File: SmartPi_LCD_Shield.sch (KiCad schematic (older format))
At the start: 47 parts, among them J1 Ant_SMA, J3 Micro_SD_Card, J4 Conn_01x02, J5 Conn_01x16, Q1 BC547, SW1 Reset, SW2 UP, SW3 LEFT, SW4 RIGHT, SW5 SELECT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

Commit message: finished routing
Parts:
- added CreativeCommonsPublicDomain1: License, Symbol:Symbol_CreativeCommonsPublicDomain_SilkScreenTop_Small, symbol Connector:TestPoint
- added J2: Conn_01x01, Connector_PinSocket_2.54mm:PinSocket_1x01_P2.54mm_Vertical, symbol Connector_Generic:Conn_01x01
- added KiCad1: License, Symbol:KiCad-Logo2_8mm_SilkScreen, symbol Connector:TestPoint
- added RV2: 10k, Potentiometer_THT:Potentiometer_Bourns_3296X_Horizontal, symbol Device:R_POT
- LOGO1: footprint Symbol:OSHW-Logo2_7.3x6mm_SilkScreen -> Symbol:OSHW-Logo2_14.6x12mm_SilkScreen
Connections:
- net +5V: now also RV2.3
- net GND: now also RV2.1
- net at DS1.3 (VO), RV1.2: now also RV2.2
- net at J1.1 (Pin_1), U1.9 (ANT): now also J2.1 (Pin_1)
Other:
- moved on the sheet: J1
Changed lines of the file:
@@
-EESchema Schematic File Version 5
+EESchema Schematic File Version 4
+LIBS:SmartPi_LCD_Shield-cache
 EELAYER 29 0
 EELAYER END
@@
 U 1 1 5CDA4BA3
 P 2750 5400
-F 0 "RV1" H 2680 5354 50  0000 R CNN
-F 1 "10k" H 2680 5445 50  0000 R CNN
+F 0 "RV1" H 2500 5450 50  0000 R CNN
+F 1 "10k" H 2500 5350 50  0000 R CNN
 F 2 "Potentiometer_THT:Potentiometer_Bourns_3266P_Horizontal" H 2750 5400 50  0001 C CNN
 F 3 "~" H 2750 5400 50  0001 C CNN
@@
 L Connector_Generic:Conn_01x02 J1
 U 1 1 5D0CF337
-P 6700 1400
-F 0 "J1" H 6618 1075 50  0000 C CNN
-F 1 "Ant_SMA" H 6618 1166 50  0000 C CNN
-F 2 "Connector_Coaxial:SMA_Amphenol_132289_EdgeMount" H 6700 1400 50  0001 C CNN
-F 3 "~" H 6700 1400 50  0001 C CNN
-	1    6700 1400
+P 7250 1400
+F 0 "J1" H 7168 1075 50  0000 C CNN
+F 1 "Ant_SMA" H 7168 1166 50  0000 C CNN
+F 2 "Connector_Coaxial:SMA_Amphenol_132289_EdgeMount" H 7250 1400 50  0001 C CNN
+F 3 "~" H 7250 1400 50  0001 C CNN
+	1    7250 1400
 	1    0    0    1
 $EndComp
@@
 L power:GND #PWR03
 U 1 1 5D0D7020
-P 6400 1100
-F 0 "#PWR03" H 6400 850 50  0001 C CNN
-F 1 "GND" V 6400 900 50  0000 C CNN
-F 2 "" H 6400 1100 50  0001 C CNN
-F 3 "" H 6400 1100 50  0001 C CNN
-	1    6400 1100
+P 6950 1100
+F 0 "#PWR03" H 6950 850 50  0001 C CNN
+F 1 "GND" V 6950 900 50  0000 C CNN
+F 2 "" H 6950 1100 50  0001 C CNN
+F 3 "" H 6950 1100 50  0001 C CNN
+	1    6950 1100
 	-1   0    0    1
 $EndComp
 Wire Wire Line
-	6500 1300 6400 1300
+	7050 1300 6950 1300
 Wire Wire Line
 	5700 3900 5250 3900
@@
 $EndComp
 Wire Wire Line
-	6250 1400 6500 1400
-Wire Wire Line
-	6400 1100 6400 1300
+	6950 1100 6950 1300
 $Comp
 L Graphic:Logo_Open_Hardware_Small LOGO1
@@
 F 0 "LOGO1" H 7300 7125 50  0001 C CNN
 F 1 "Logo_Open_Hardware_Small" H 7300 6625 50  0001 C CNN
-F 2 "Symbol:OSHW-Logo2_7.3x6mm_SilkScreen" H 7300 6850 50  0001 C CNN
+F 2 "Symbol:OSHW-Logo2_14.6x12mm_SilkScreen" H 7300 6850 50  0001 C CNN
 F 3 "~" H 7300 6850 50  0001 C CNN
 	1    7300 6850
 	1    0    0    -1
 $EndComp
+$Comp
+L Connector_Generic:Conn_01x01 J2
+U 1 1 5CD99C08
+P 6500 1050
+F 0 "J2" V 6418 962 50  0000 R CNN
+F 1 "Conn_01x01" V 6373 962 50  0001 R CNN
+F 2 "Connector_PinSocket_2.54mm:PinSocket_1x01_P2.54mm_Vertical" H 6500 1050 50  0001 C CNN
+F 3 "~" H 6500 1050 50  0001 C CNN
+	1    6500 1050
+	0    -1   -1   0
+$EndComp
+Wire Wire Line
+	6250 1400 6500 1400
+Wire Wire Line
+	6500 1250 6500 1400
+Connection ~ 6500 1400
+Wire Wire Line
+	6500 1400 7050 1400
+$Comp
+L Device:R_POT RV2
+U 1 1 5CDAF2AC
+P 2750 5400
+F 0 "RV2" H 2680 5354 50  0000 R CNN
+F 1 "10k" H 2680 5445 50  0000 R CNN
+F 2 "Potentiometer_THT:Potentiometer_Bourns_3296X_Horizontal" H 2750 5400 50  0001 C CNN
+F 3 "~" H 2750 5400 50  0001 C CNN
+	1    2750 5400
+	-1   0    0    -1
+$EndComp
+Connection ~ 2750 5250
+Connection ~ 2600 5400
+Connection ~ 2750 5550
+$Comp
+L Connector:TestPoint CreativeCommonsPublicDomain1
+U 1 1 5CDBC513
+P 8000 6800
+F 0 "CreativeCommonsPublicDomain1" H 8058 6872 50  0000 L CNN
+F 1 "License" H 8058 6827 50  0001 L CNN
+F 2 "Symbol:Symbol_CreativeCommonsPublicDomain_SilkScreenTop_Small" H 8200 6800 50  0001 C CNN
+F 3 "~" H 8200 6800 50  0001 C CNN
+	1    8000 6800
+	1    0    0    -1
+$EndComp
+$Comp
+L Connector:TestPoint KiCad1
+U 1 1 5CDBD805
+P 8000 7050
+F 0 "KiCad1" H 8058 7122 50  0000 L CNN
+F 1 "License" H 8058 7077 50  0001 L CNN
+F 2 "Symbol:KiCad-Logo2_8mm_SilkScreen" H 8200 7050 50  0001 C CNN
+F 3 "~" H 8200 7050 50  0001 C CNN
+	1    8000 7050
+	1    0    0    -1
+$EndComp

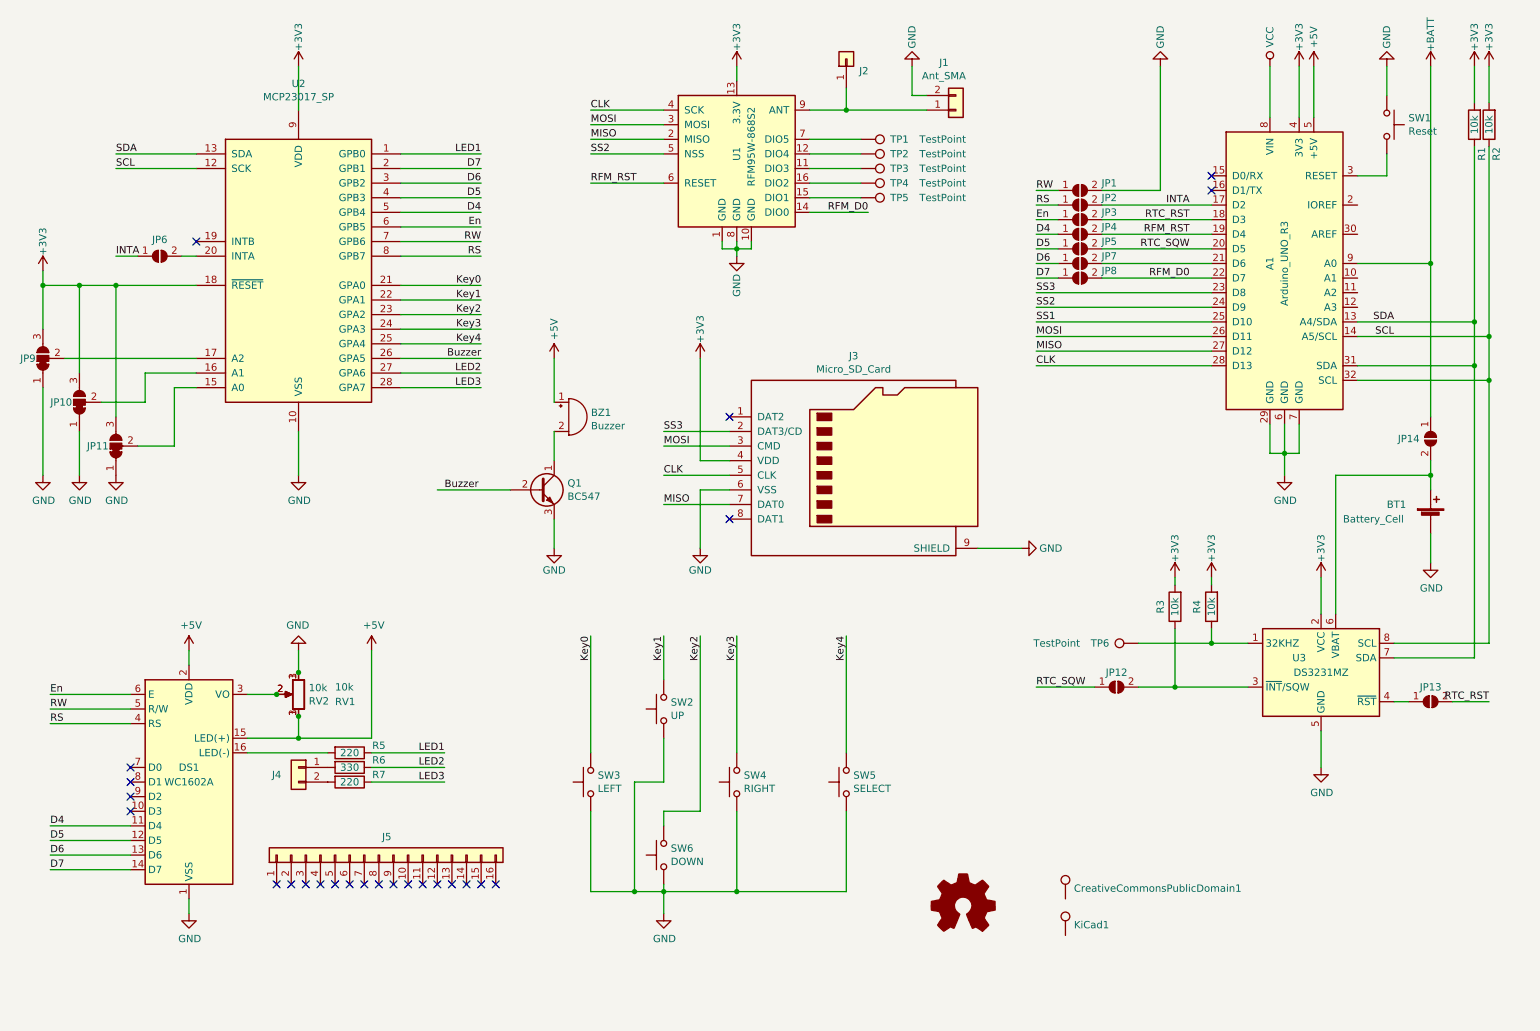
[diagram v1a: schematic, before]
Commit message: added hexbuffer for sd card
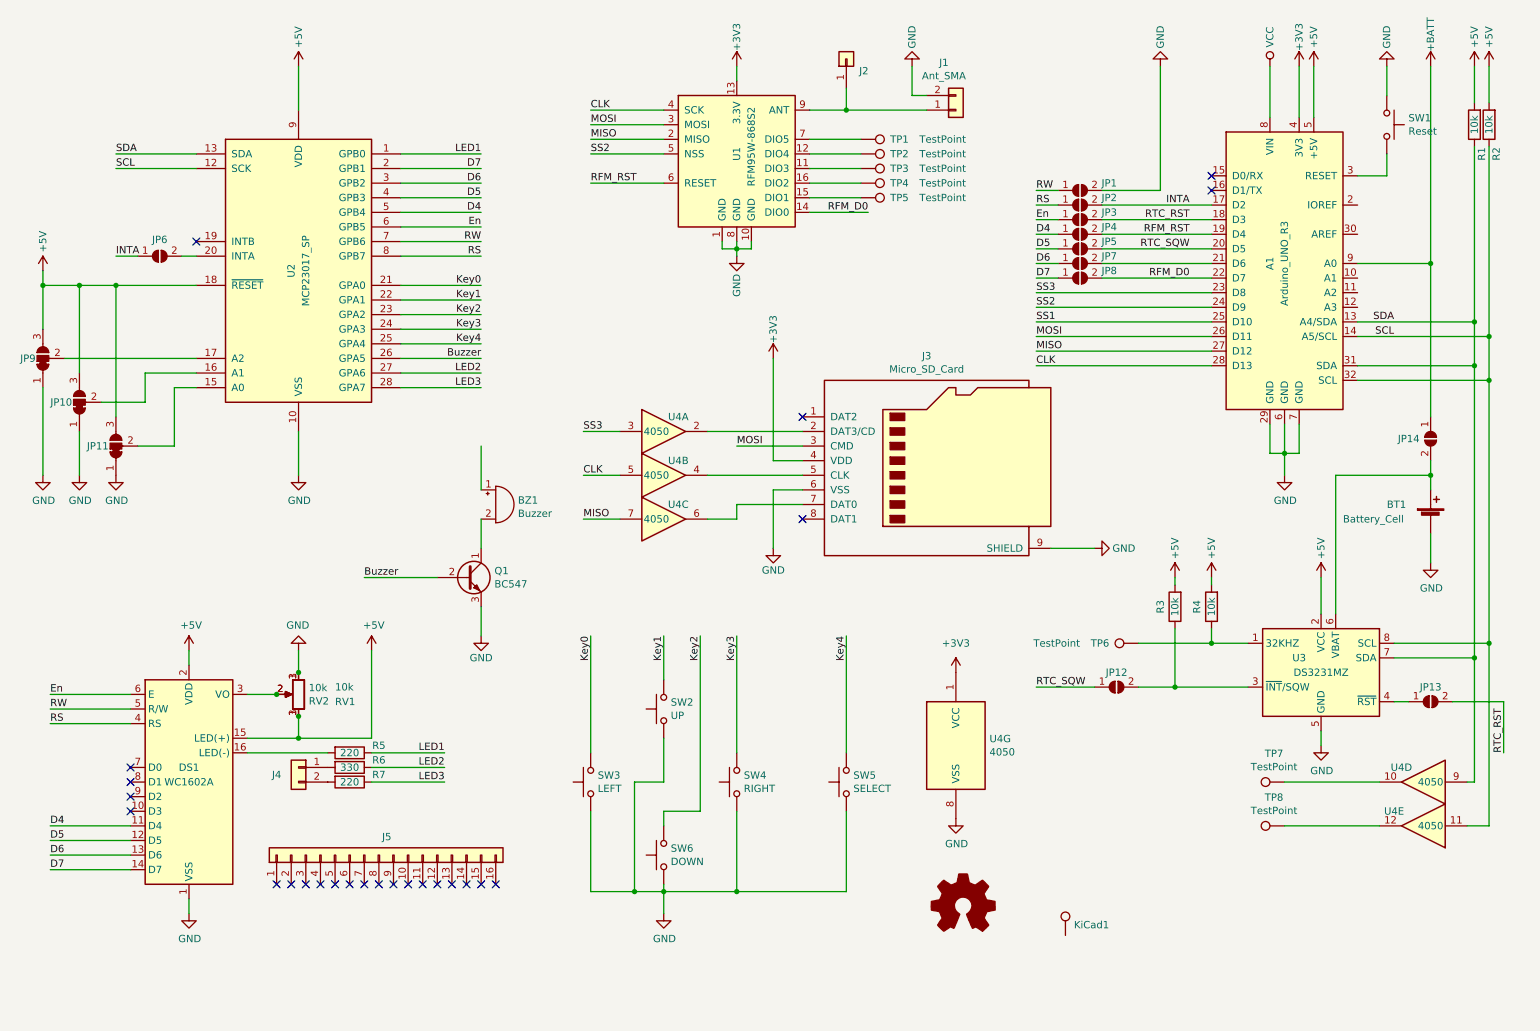
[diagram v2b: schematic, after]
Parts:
- removed CreativeCommonsPublicDomain1: License, Symbol:Symbol_CreativeCommonsPublicDomain_SilkScreenTop_Small, symbol Connector:TestPoint
- added TP7, TP8: TestPoint, TestPoint:TestPoint_Pad_D1.5mm, symbol Connector:TestPoint
- added U4: 4050, Package_SO:SOIC-16_3.9x9.9mm_P1.27mm, symbol 4xxx:4050
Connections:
- net +3V3: now also U4.1 (VCC); no longer JP10.3 (B), JP11.3 (B), JP9.3 (B), R1.2, R2.2, R3.2, R4.2, U2.18 (~RESET~), U2.9 (VDD), U3.2 (VCC)
- net +5V: now also JP10.3 (B), JP11.3 (B), JP9.3 (B), R1.2, R2.2, R3.2, R4.2, U2.18 (~RESET~), U2.9 (VDD), U3.2 (VCC); no longer BZ1.1 (-)
- net CLK: now also U4.5; no longer J3.5 (CLK)
- net GND: now also U4.8 (VSS)
- net MISO: now also U4.7; no longer J3.7 (DAT0)
- net SCL: now also U4.11
- net SDA: now also U4.9
- net SS3: now also U4.3; no longer J3.2 (DAT3/CD)
- new net: J3.2 (DAT3/CD), U4.2
- new net: J3.5 (CLK), U4.4
- new net: TP7.1, U4.10
- new net: TP8.1, U4.12
- new net: J3.7 (DAT0), U4.6
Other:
- moved on the sheet: BZ1, J3, Q1

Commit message: routing complete with hex buffer
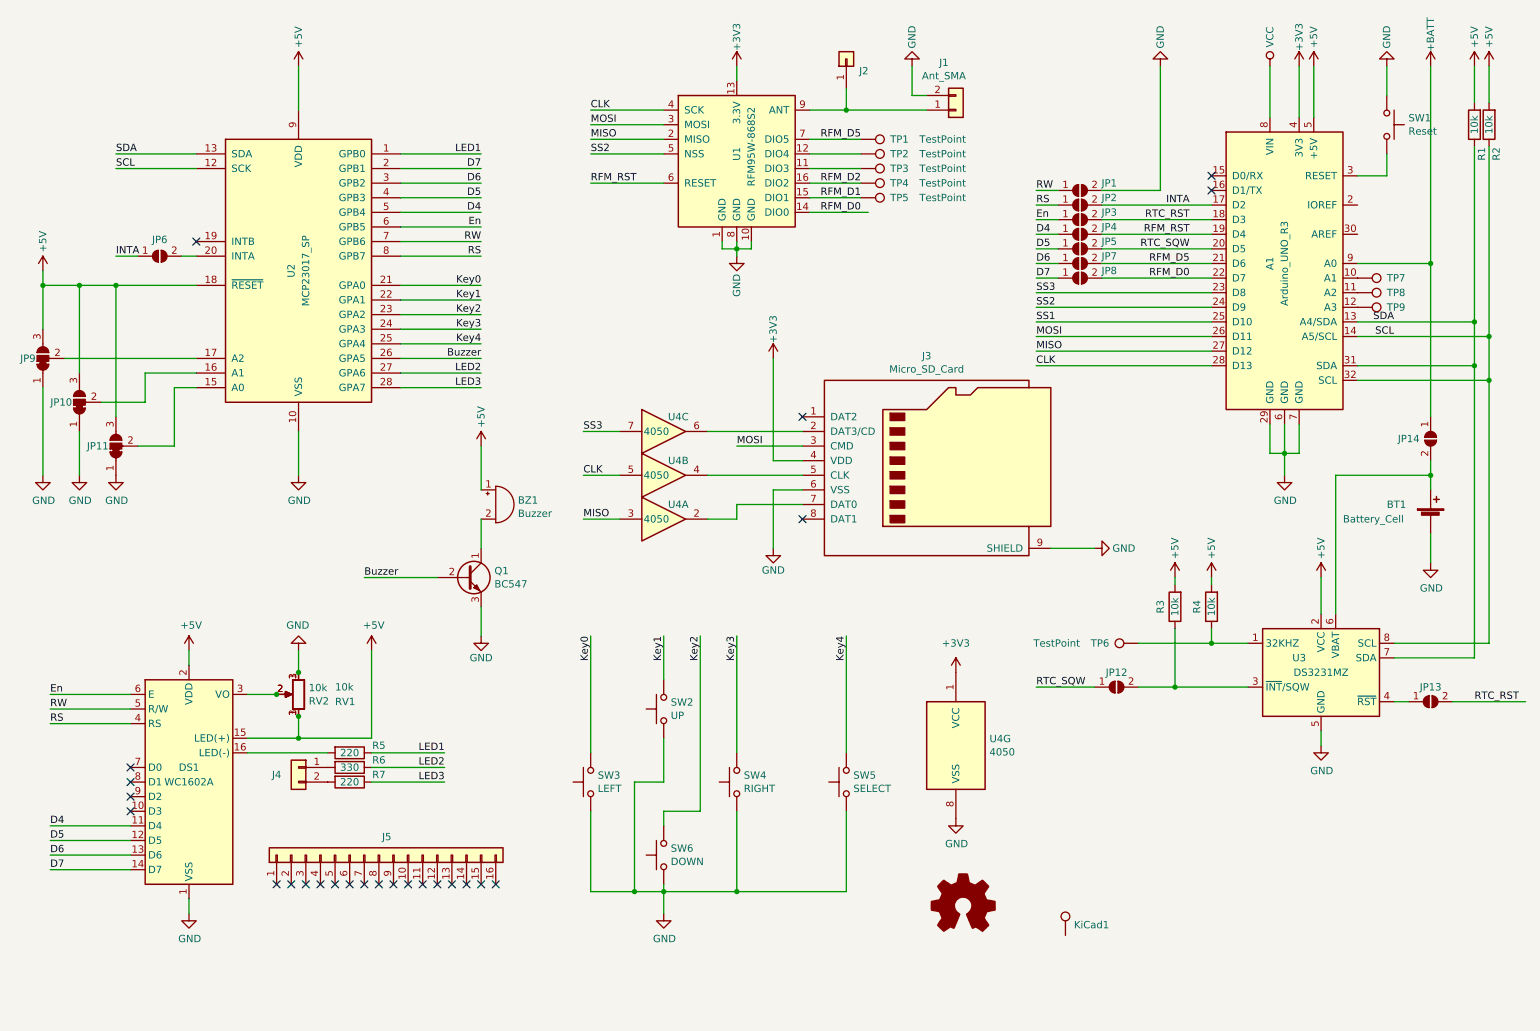
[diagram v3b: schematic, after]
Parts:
- removed unit 4 of U4
- removed unit 5 of U4
- added TP9: TestPoint, TestPoint:TestPoint_Pad_D2.0mm, symbol Connector:TestPoint
- TP7, TP8: footprint TestPoint:TestPoint_Pad_D1.5mm -> TestPoint:TestPoint_Pad_D2.0mm
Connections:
- net +5V: now also BZ1.1 (-)
- net MISO: now also U4.3; no longer U4.7
- net SS3: now also U4.7; no longer U4.3
- net at A1.10 (A1): now also TP7.1
- net at A1.11 (A2): now also TP8.1
- net at A1.12 (A3): now also TP9.1
- net RFM_D5: now reaches A1.21 (D6), JP7.2 (B)
- net RFM_D5: now also TP1.1, U1.7 (DIO5)
- net at U4.2: now also J3.7 (DAT0); no longer J3.2 (DAT3/CD)
- net at U4.6: now also J3.2 (DAT3/CD); no longer J3.7 (DAT0)
- net RFM_D1: now reaches TP5.1, U1.15 (DIO1)
- net RFM_D2: now reaches TP4.1, U1.16 (DIO2)
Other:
- moved on the sheet: U4A, U4C
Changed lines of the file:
@@
-EESchema Schematic File Version 5
+EESchema Schematic File Version 4
 LIBS:SmartPi_LCD_Shield-cache
 EELAYER 29 0
@@
 Text Label 4750 1900 0    50   ~ 0
 RFM_RST
-Text Label 6650 2100 2    50   ~ 0
+Text Label 6600 2100 2    50   ~ 0
 RFM_D0
 Wire Wire Line
@@
 Text Label 8850 2350 2    50   ~ 0
 RTC_SQW
-Text Label 11000 5800 1    50   ~ 0
+Text Label 10800 5450 0    50   ~ 0
 RTC_RST
 Text Label 8850 2150 2    50   ~ 0
@@
 L 4xxx:4050 U4
 U 1 1 5CE43B90
-P 5250 3600
-F 0 "U4" H 5350 3700 50  0000 C CNN
-F 1 "4050" H 5200 3600 50  0000 C CNN
-F 2 "Package_SO:SOIC-16_3.9x9.9mm_P1.27mm" H 5250 3600 50  0001 C CNN
-F 3 "http://www.intersil.com/content/dam/intersil/documents/cd40/cd4050bms.pdf" H 5250 3600 50  0001 C CNN
-	1    5250 3600
+P 5250 4200
+F 0 "U4" H 5350 4300 50  0000 C CNN
+F 1 "4050" H 5200 4200 50  0000 C CNN
+F 2 "Package_SO:SOIC-16_3.9x9.9mm_P1.27mm" H 5250 4200 50  0001 C CNN
+F 3 "http://www.intersil.com/content/dam/intersil/documents/cd40/cd4050bms.pdf" H 5250 4200 50  0001 C CNN
+	1    5250 4200
 	1    0    0    -1
 $EndComp
@@
 L 4xxx:4050 U4
 U 3 1 5CE486A7
-P 5250 4200
-F 0 "U4" H 5350 4300 50  0000 C CNN
-F 1 "4050" H 5200 4200 50  0000 C CNN
-F 2 "Package_SO:SOIC-16_3.9x9.9mm_P1.27mm" H 5250 4200 50  0001 C CNN
-F 3 "http://www.intersil.com/content/dam/intersil/documents/cd40/cd4050bms.pdf" H 5250 4200 50  0001 C CNN
-	3    5250 4200
-	1    0    0    -1
-$EndComp
-$Comp
-L 4xxx:4050 U4
-U 4 1 5CE48D58
-P 10450 6000
-F 0 "U4" H 10600 5900 50  0000 C CNN
-F 1 "4050" H 10400 6000 50  0000 C CNN
-F 2 "Package_SO:SOIC-16_3.9x9.9mm_P1.27mm" H 10450 6000 50  0001 C CNN
-F 3 "http://www.intersil.com/content/dam/intersil/documents/cd40/cd4050bms.pdf" H 10450 6000 50  0001 C CNN
-	4    10450 6000
-	-1   0    0    1
+P 5250 3600
+F 0 "U4" H 5350 3700 50  0000 C CNN
+F 1 "4050" H 5200 3600 50  0000 C CNN
+F 2 "Package_SO:SOIC-16_3.9x9.9mm_P1.27mm" H 5250 3600 50  0001 C CNN
+F 3 "http://www.intersil.com/content/dam/intersil/documents/cd40/cd4050bms.pdf" H 5250 3600 50  0001 C CNN
+	3    5250 3600
+	1    0    0    -1
 $EndComp
 Wire Wire Line
@@
 $EndComp
 $Comp
-L 4xxx:4050 U4
-U 5 1 5CE5FA53
-P 10450 6300
-F 0 "U4" H 10650 6200 50  0000 C CNN
-F 1 "4050" H 10400 6300 50  0000 C CNN
-F 2 "Package_SO:SOIC-16_3.9x9.9mm_P1.27mm" H 10450 6300 50  0001 C CNN
-F 3 "http://www.intersil.com/content/dam/intersil/documents/cd40/cd4050bms.pdf" H 10450 6300 50  0001 C CNN
-	5    10450 6300
-	-1   0    0    1
-$EndComp
-Wire Wire Line
-	11000 5450 11000 5800
-Wire Wire Line
-	10650 5450 11000 5450
-Wire Wire Line
-	10800 5150 10800 6000
-Wire Wire Line
-	10800 6000 10750 6000
-Connection ~ 10800 5150
-Wire Wire Line
-	10900 5050 10900 6300
-Wire Wire Line
-	10900 6300 10750 6300
-Connection ~ 10900 5050
-$Comp
 L power:+5V #PWR0104
 U 1 1 5CE6DFC4
@@
 	9750 5750 9750 5650
 $Comp
-L Connector:TestPoint TP7
-U 1 1 5CE480C5
-P 9500 6000
-F 0 "TP7" V 9695 6072 50  0000 C CNN
-F 1 "TestPoint" V 9604 6072 50  0000 C CNN
-F 2 "TestPoint:TestPoint_Pad_D1.5mm" H 9700 6000 50  0001 C CNN
-F 3 "~" H 9700 6000 50  0001 C CNN
-	1    9500 6000
-	0    -1   -1   0
-$EndComp
-$Comp
-L Connector:TestPoint TP8
-U 1 1 5CE4867F
-P 9500 6300
-F 0 "TP8" V 9695 6372 50  0000 C CNN
-F 1 "TestPoint" V 9604 6372 50  0000 C CNN
-F 2 "TestPoint:TestPoint_Pad_D1.5mm" H 9700 6300 50  0001 C CNN
-F 3 "~" H 9700 6300 50  0001 C CNN
-	1    9500 6300
-	0    -1   -1   0
-$EndComp
-Wire Wire Line
-	9500 6300 10150 6300
-Wire Wire Line
-	9500 6000 10150 6000
-$Comp
 L power:+5V #PWR0110
 U 1 1 5CE4AB80
@@
 	1    0    0    -1
 $EndComp
+Wire Wire Line
+	10650 5450 11150 5450
+$Comp
+L power:+5V #PWR0111
+U 1 1 5CE6A151
+P 4000 3700
+F 0 "#PWR0111" H 4000 3550 50  0001 C CNN
+F 1 "+5V" V 4000 3900 50  0000 C CNN
+F 2 "" H 4000 3700 50  0001 C CNN
+F 3 "" H 4000 3700 50  0001 C CNN
+	1    4000 3700
+	1    0    0    -1
+$EndComp
+Text Label 6600 1600 2    50   ~ 0
+RFM_D5
+Text Label 8850 2450 2    50   ~ 0
+RFM_D5
+Text Label 6600 2000 2    50   ~ 0
+RFM_D1
+Text Label 6600 1900 2    50   ~ 0
+RFM_D2
+$Comp
+L Connector:TestPoint TP9
+U 1 1 5CE6B5D7
+P 10000 2750
+F 0 "TP9" V 10000 2950 50  0000 L CNN
+F 1 "TestPoint" V 10000 3150 50  0001 L CNN
+F 2 "TestPoint:TestPoint_Pad_D2.0mm" H 10200 2750 50  0001 C CNN
+F 3 "~" H 10200 2750 50  0001 C CNN
+	1    10000 2750
+	0    1    1    0
+$EndComp
+$Comp
+L Connector:TestPoint TP8
+U 1 1 5CE6BC9E
+P 10000 2650
+F 0 "TP8" V 10000 2850 50  0000 L CNN
+F 1 "TestPoint" V 10000 3050 50  0001 L CNN
+F 2 "TestPoint:TestPoint_Pad_D2.0mm" H 10200 2650 50  0001 C CNN
+F 3 "~" H 10200 2650 50  0001 C CNN
+	1    10000 2650
+	0    1    1    0
+$EndComp
+$Comp
+L Connector:TestPoint TP7
+U 1 1 5CE6BF48
+P 10000 2550
+F 0 "TP7" V 10000 2750 50  0000 L CNN
+F 1 "TestPoint" V 10000 2950 50  0001 L CNN
+F 2 "TestPoint:TestPoint_Pad_D2.0mm" H 10200 2550 50  0001 C CNN
+F 3 "~" H 10200 2550 50  0001 C CNN
+	1    10000 2550
+	0    1    1    0
+$EndComp
 $EndSCHEMATC
